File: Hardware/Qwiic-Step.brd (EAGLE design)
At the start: 44.5 x 44.5 mm, 76 parts, among them J1 PTH, J2 Qwiic Right Angle, J3 POWER_JACKSUPER_BOMB_DIGITY, J4 Qwiic Right Angle, J5 ISP, U1 A49885MM, U2 ATMEGA328P_TQFP, Y1 16MHz

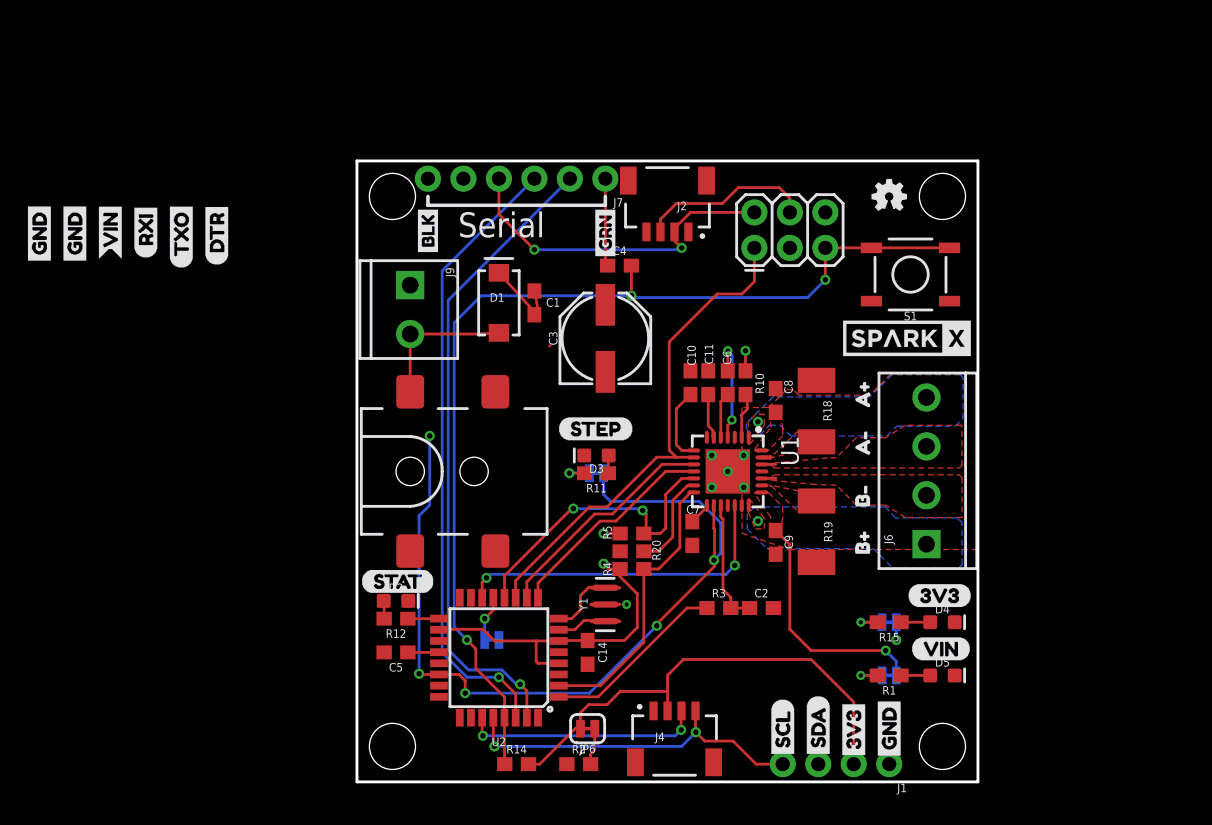
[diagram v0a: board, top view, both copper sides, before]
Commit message: New board layout. Added current sense.
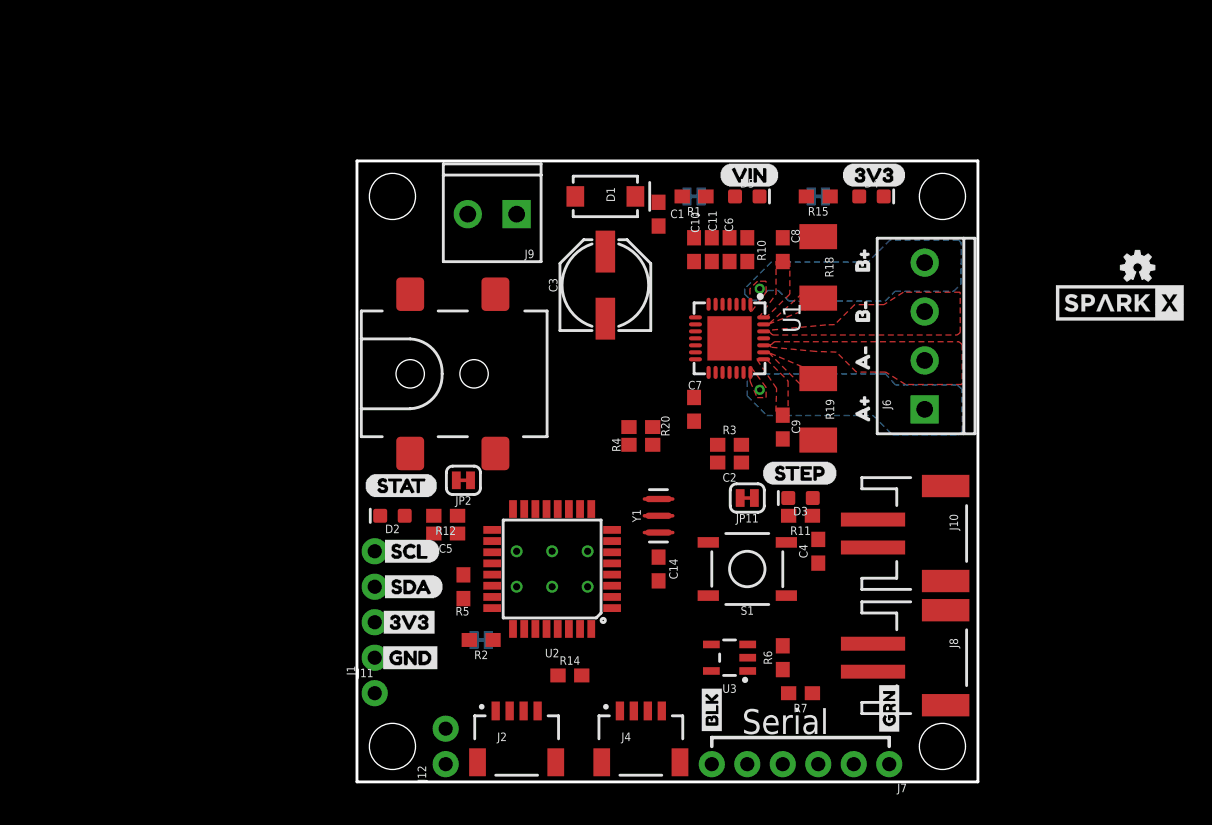
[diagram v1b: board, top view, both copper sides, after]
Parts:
- removed U$10, U$11: (no value), buzzard_labels (14):GND1
- removed U$12: (no value), buzzard_labels (14):RXI3
- removed U$13: (no value), buzzard_labels (14):TXO4
- removed U$14: (no value), buzzard_labels (14):VIN2
- removed U$9: (no value), buzzard_labels (14):DTR5
- added J10, J8: (no value), SparkFun-Connectors:JST-2-SMD
- added J11: (no value), SparkFun-Connectors:1X01_NO_SILK
- added J12: (no value), SparkFun-Connectors:1X02_NO_SILK
- added R6, R7: (no value), SparkFun-Resistors:0603
- added U3: HV7800, SparkFun-IC-Special-Function:SOT23-5
- J5: device SparkFun-Connectors:2X3 -> SparkFun-Connectors:2X3_TEST_POINTS
- moved J7 46.6 mm to (38.1, 1.27)
- moved U$21 40.1 mm to (25.4, 3.81)
- moved U$20 39.9 mm to (25.4, 3.17)
- moved U$22 39.9 mm to (38.1, 3.81)
- moved U$28 39.6 mm to (38.1, 3.17)
- moved J1 37.6 mm to (1.27, 8.89), turned to 90 degrees
- moved U$3 37.5 mm to (1.40, 8.89), turned to 0 degrees
- moved D5 37.0 mm to (27.9, 41.9)
- moved JP1 37.0 mm to (24.1, 41.9)
- moved R1 37.0 mm to (24.1, 41.9)
- moved U$8 36.6 mm to (25.9, 43.4)
- moved J2 35.9 mm to (11.4, 5.08), turned to 0 degrees
- moved U$2 35.6 mm to (1.40, 11.4), turned to 0 degrees
- moved U$6 33.9 mm to (1.52, 14.0), turned to 0 degrees
- moved U$5 32.6 mm to (1.52, 16.5), turned to 0 degrees
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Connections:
- removed net !RESET!: R5.1, U1.12, U2.12
- new net A49885_!RESET!: R5.1, U1.12, U2.22
- new net CURR_SENSE: U2.19, U3.5
- new net EP: J12.2, U2.25
- new net INT0: J8.1, U2.32
- new net INT1: J10.1, U2.1
- new net MISO: J5.1, U2.16
- new net N$6: R6.1, R7.2, U3.1
- net !ENABLE!: now also J5.4, U2.14; no longer U2.15
- net ADR: now also U2.15; no longer U2.13
- net CUR_REF_PWM: now also U2.9; no longer U2.1
- net DIR: now also U2.26; no longer U2.14
- net GND: now also J10.2, J12.1, J8.2, R7.1, U3.4
- net INT: now also J11.1, U2.24; no longer U2.32
- net MS1: now also U2.13; no longer J5.1, U2.11
- net MS2: now also U2.12; no longer U2.10
- net MS3: now also U2.11; no longer U2.9
- net SCK: now also J5.3
- net SCL: no longer J5.3
- net SDA: no longer J5.4
- net STEP: now also U2.10; no longer U2.22
- net VIN: now also R6.2, U3.3
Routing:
- net 3.3V: track 89.2 -> 0.00 mm, vias 6 -> 0
- net !RST!: track 74.4 -> 0.00 mm, vias 3 -> 0
- net STEP: track 61.4 -> 0.00 mm, vias 5 -> 0
- net TXO: track 46.1 -> 0.00 mm, vias 1 -> 0
- net RXI: track 44.8 -> 0.00 mm, vias 1 -> 0
- net MS1: track 36.4 -> 0.00 mm
- net SDA: track 29.5 -> 0.00 mm, vias 2 -> 0
- net SCL: track 25.7 -> 0.00 mm, vias 2 -> 0
- net DIR: track 24.0 -> 0.00 mm, vias 2 -> 0
- net VIN: track 22.8 -> 0.00 mm, vias 1 -> 0
- net !RESET!: track 21.9 -> 0.00 mm, vias 2 -> 0
- net !SLEEP!: track 20.3 -> 0.00 mm
- net MS2: track 16.6 -> 0.00 mm
- net MS3: track 15.5 -> 0.00 mm
- net CUR_REF_PWM: track 13.2 -> 0.00 mm
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- removed copper zone on layer 1, net GND
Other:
- board text removed: "THIS IS A 4-LAYER BOARD."

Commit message: Removed generated libraries and finishing up layout
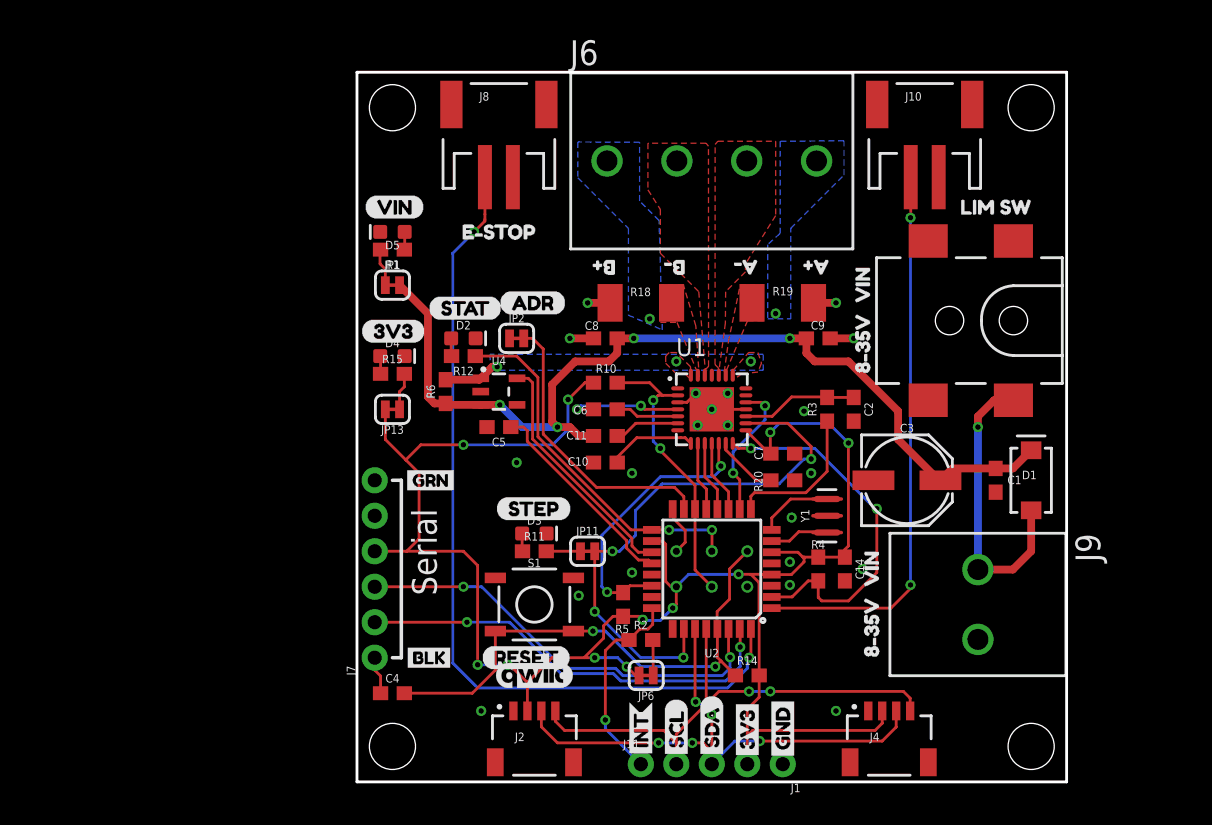
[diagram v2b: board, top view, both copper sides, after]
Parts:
- removed J12: (no value), SparkFun-Connectors:1X02_NO_SILK
- removed R7: (no value), SparkFun-Resistors:0603
- removed U3: HV7800, SparkFun-IC-Special-Function:SOT23-5
- added U$10, U$11: (no value), buzzard_labels (16):8#35V0
- added U$12, U$13: (no value), buzzard_labels (16):VIN1
- added U$14: (no value), buzzard_labels (16):E#STOP2
- added U$23: (no value), buzzard_labels (16):LIM_SW3
- added U$24: (no value), buzzard_labels (16):INT4
- added U$25: (no value), buzzard_labels (18):ADR0
- added U$26: (no value), buzzard_labels (18):QWIIC_STEP2
- added U$27: (no value), buzzard_labels (18):RESET1
- added U$9: (no value), SparkFun-Aesthetics:QWIIC_5.5MM
- added U4: HV7801, SparkFun-IC-Special-Function:SOT23-5
- J3: value POWER_JACKSUPER_BOMB_DIGITY -> 5.5x2.1mm Barrel; device Testing:POWER_JACK_SMD_OVERPASTE_SUPER_BOMB_DIGITY -> SparkFun-Connectors:POWER_JACK_SMD
- J6: device SparkFun-Connectors:SCREWTERMINAL-3.5MM-4 -> SparkFun-Connectors:LATCHTERMINAL-5MM-4
- J9: device SparkFun-Connectors:SCREWTERMINAL-3.5MM-2 -> SparkFun-Connectors:LATCHTERMINAL-5MM-2
- JP10, JP7, JP8, JP9: device SparkFun-7-28-09:STAND-OFF -> SparkFun-Hardware:STAND-OFF
- U1: value A49885MM -> A4988ALT1; device SparkFun-PowerIC:QFN-28-5MM -> SparkFun-IC-Special-Function:QFN-28-5MM
- moved J8 48.8 mm to (10.2, 47.0), turned to 0 degrees
- moved J3 43.3 mm to (47.0, 33.0), turned to 180 degrees
- moved J9 43.3 mm to (44.5, 12.7), turned to 270 degrees
- moved LOGO1 41.2 mm to (33.0, 2.54), flipped to the bottom
- moved U$28 39.5 mm to (3.17, 21.6), turned to 0 degrees
- moved J7 37.6 mm to (1.27, 8.89), turned to 90 degrees
- moved D1 36.6 mm to (48.3, 21.6), turned to 90 degrees
- moved U$1 36.2 mm to (0.25, 32.3)
- moved D4 36.1 mm to (2.54, 30.5)
- moved U$22 35.3 mm to (7.62, 21.6), turned to 0 degrees
- moved U$19 35.2 mm to (39.4, 2.54), flipped to the bottom
- moved JP13 34.1 mm to (2.54, 26.7), flipped to the top
- moved R15 33.0 mm to (2.54, 29.2), turned to 0 degrees
- moved C4 32.1 mm to (2.54, 6.35), turned to 0 degrees
- moved C1 30.7 mm to (45.7, 21.6)
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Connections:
- removed net N$6: R6.1, R7.2, U3.1
- new net MOTOR_SUPPLY: R6.2, U1.22, U1.28, U4.1
- net COILA+: now also J6.4; no longer J6.1
- net COILA-: now also J6.3; no longer J6.2
- net COILB+: now also J6.1; no longer J6.4
- net COILB-: now also J6.2; no longer J6.3
- net CURR_SENSE: now also U4.5; no longer U3.5
- net DIR: now also U2.10; no longer U2.26
- net EP: no longer J12.2
- net GND: now also J9.2, U4.4; no longer J12.1, J9.1, R7.1, U3.4
- net N$7: now also J9.1; no longer J9.2
- net STEP: now also U2.26; no longer U2.10
- net VIN: now also R6.1, U4.3; no longer R6.2, U1.22, U1.28, U3.3
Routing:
- net 3.3V: track 0.00 -> 133.4 mm, vias 0 -> 11
- net VIN: track 0.00 -> 68.7 mm, vias 0 -> 4
- net INT0: track 0.00 -> 61.1 mm, vias 0 -> 2
- net INT1: track 0.00 -> 40.0 mm, vias 0 -> 2
- net SDA: track 0.00 -> 39.9 mm, vias 0 -> 5
- net STEP: track 0.00 -> 39.6 mm, vias 0 -> 4
- net !RST!: track 0.00 -> 37.7 mm, vias 0 -> 2
- net SCL: track 0.00 -> 36.7 mm, vias 0 -> 2
- net RXI: track 0.00 -> 31.1 mm, vias 0 -> 2
- net TXO: track 0.00 -> 31.0 mm, vias 0 -> 2
- net !SLEEP!: track 0.00 -> 26.9 mm, vias 0 -> 2
- net SCK: track 0.00 -> 26.3 mm, vias 0 -> 2
- net N$7: track 0.00 -> 21.3 mm, vias 0 -> 1
- net ADR: track 0.00 -> 20.6 mm
- net !ENABLE!: track 0.00 -> 20.6 mm, vias 0 -> 2
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- added copper zone on layer 1, net GND
- added copper zone on layer 1, net MOTOR_SUPPLY
- added copper zone on layer 16, net MOTOR_SUPPLY
- added copper zone on layer 1, net N$21
- removed copper zone on layer 1, net COILA+
- removed copper zone on layer 1, net COILB+
- removed copper zone on layer 1, net N$31
- removed copper zone on layer 1, net VIN
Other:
- board size 44.5 x 44.5 mm -> 50.8 x 50.8 mm

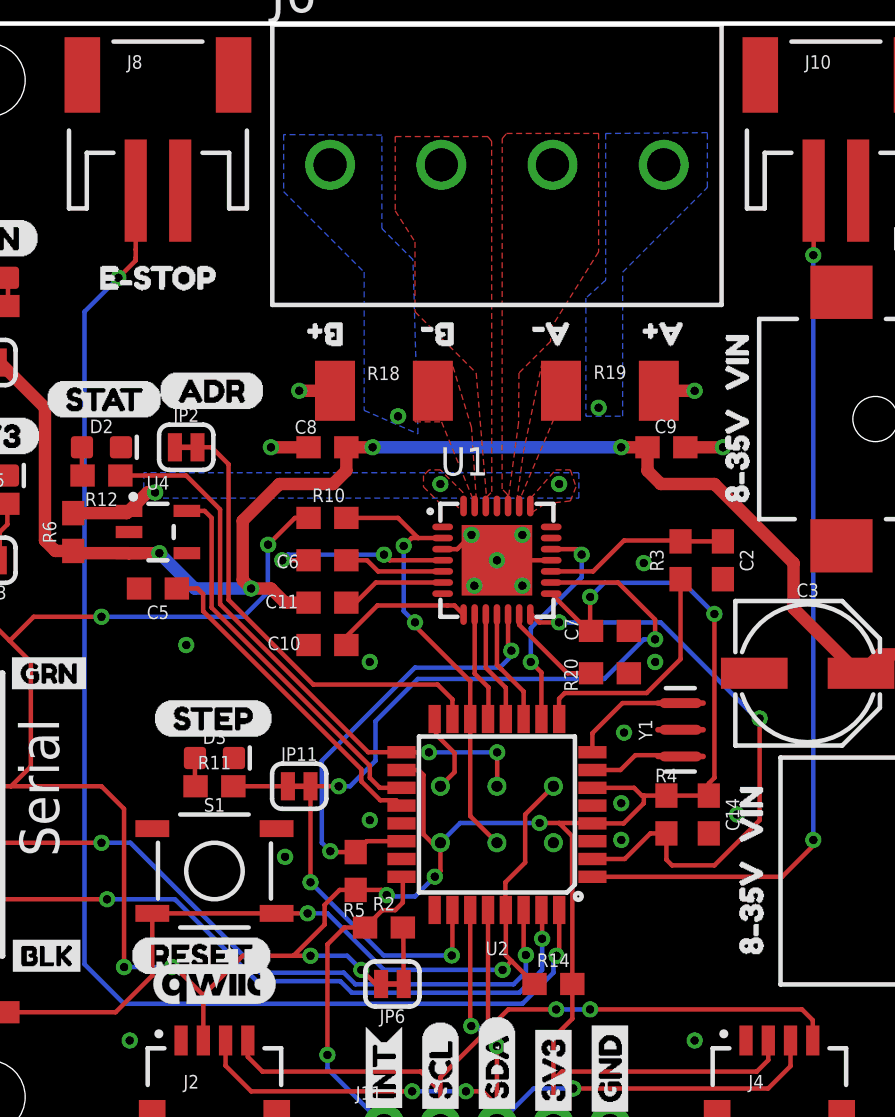
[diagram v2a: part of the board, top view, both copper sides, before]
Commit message: Changes to polygon classes
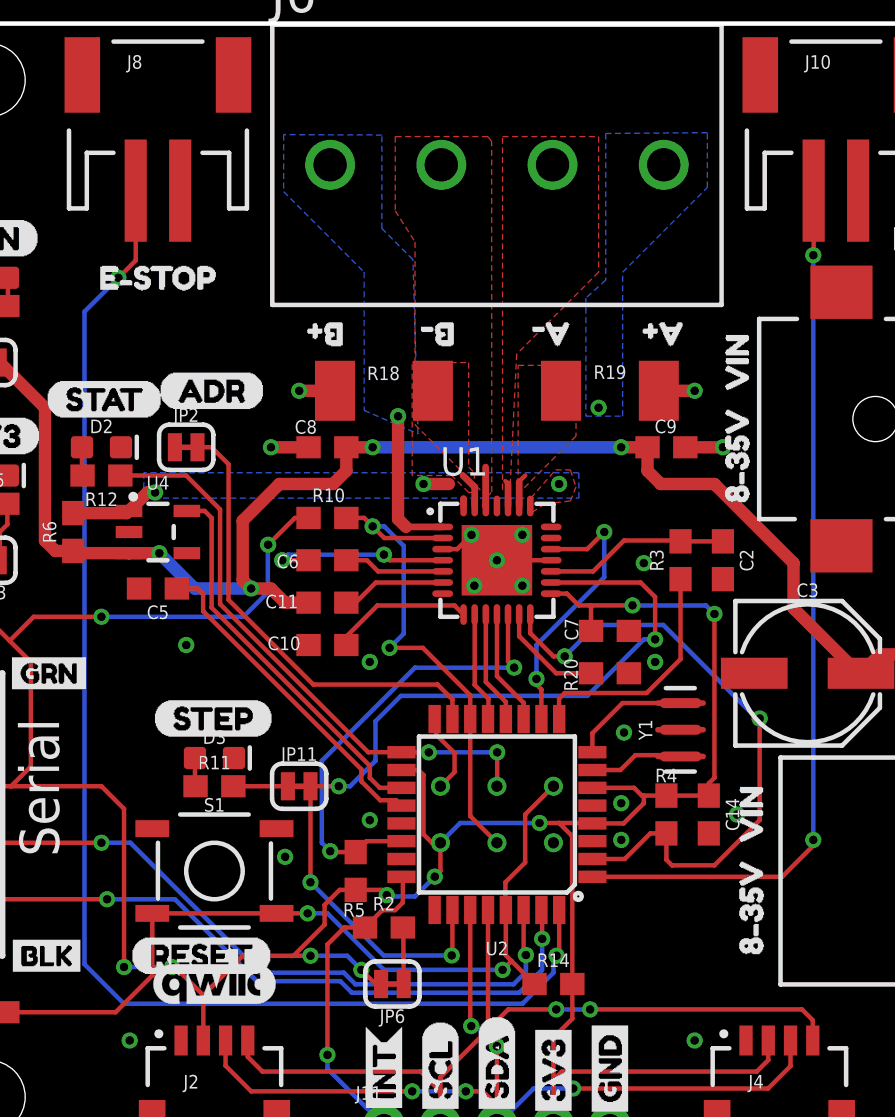
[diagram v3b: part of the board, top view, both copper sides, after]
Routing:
- net COILB+: track 0.00 -> 6.77 mm
- net DIR: track 10.0 -> 12.5 mm
- net !ENABLE!: track 20.6 -> 22.9 mm
- net COILB-: track 0.00 -> 1.75 mm
- net !SLEEP!: track 26.9 -> 28.6 mm
- net N$31: track 0.00 -> 1.59 mm
- net N$32: track 0.00 -> 1.48 mm
- net MOTOR_SUPPLY: track 4.07 -> 5.54 mm
- net 3.3V: track 133.4 -> 132.0 mm
- net COILA-: track 0.00 -> 1.17 mm
- net STEP: track 39.6 -> 40.2 mm
- added copper zone on layer 1, net N$31
- removed copper zone on layer 1, net N$21
